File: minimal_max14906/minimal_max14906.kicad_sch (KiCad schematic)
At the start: 75 parts, among them J1 CLP-114-02-G-D-BE, J2 CLP-102-02-G-D-BE, J3 CLP-102-02-G-D-BE, J4 CLP-102-02-G-D-BE, J6 CLP-102-02-G-D-BE, J7 CLP-102-02-G-D-BE, J8 CLP-102-02-G-D-BE, Q1 SI7309DN-T1-E3, Q2 SI7309DN-T1-E3, Q3 SI7309DN-T1-E3, Q4 SI7309DN-T1-E3, U1 MAX14906ATM+

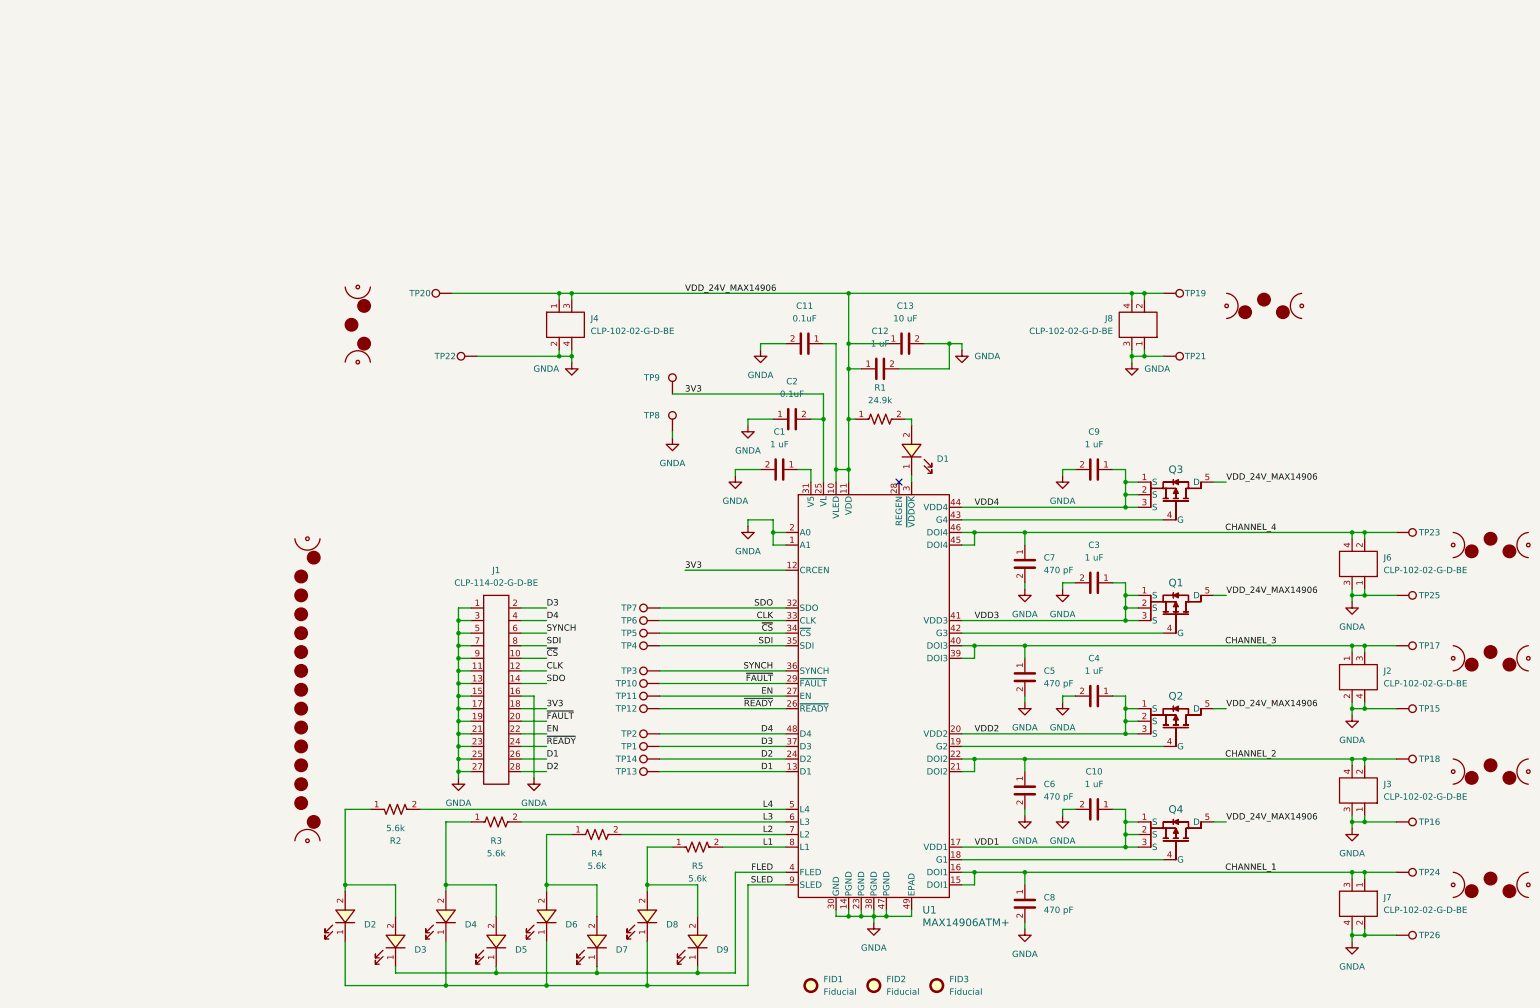
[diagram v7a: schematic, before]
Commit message: Update KiCAD schematic references for consistency and accuracy
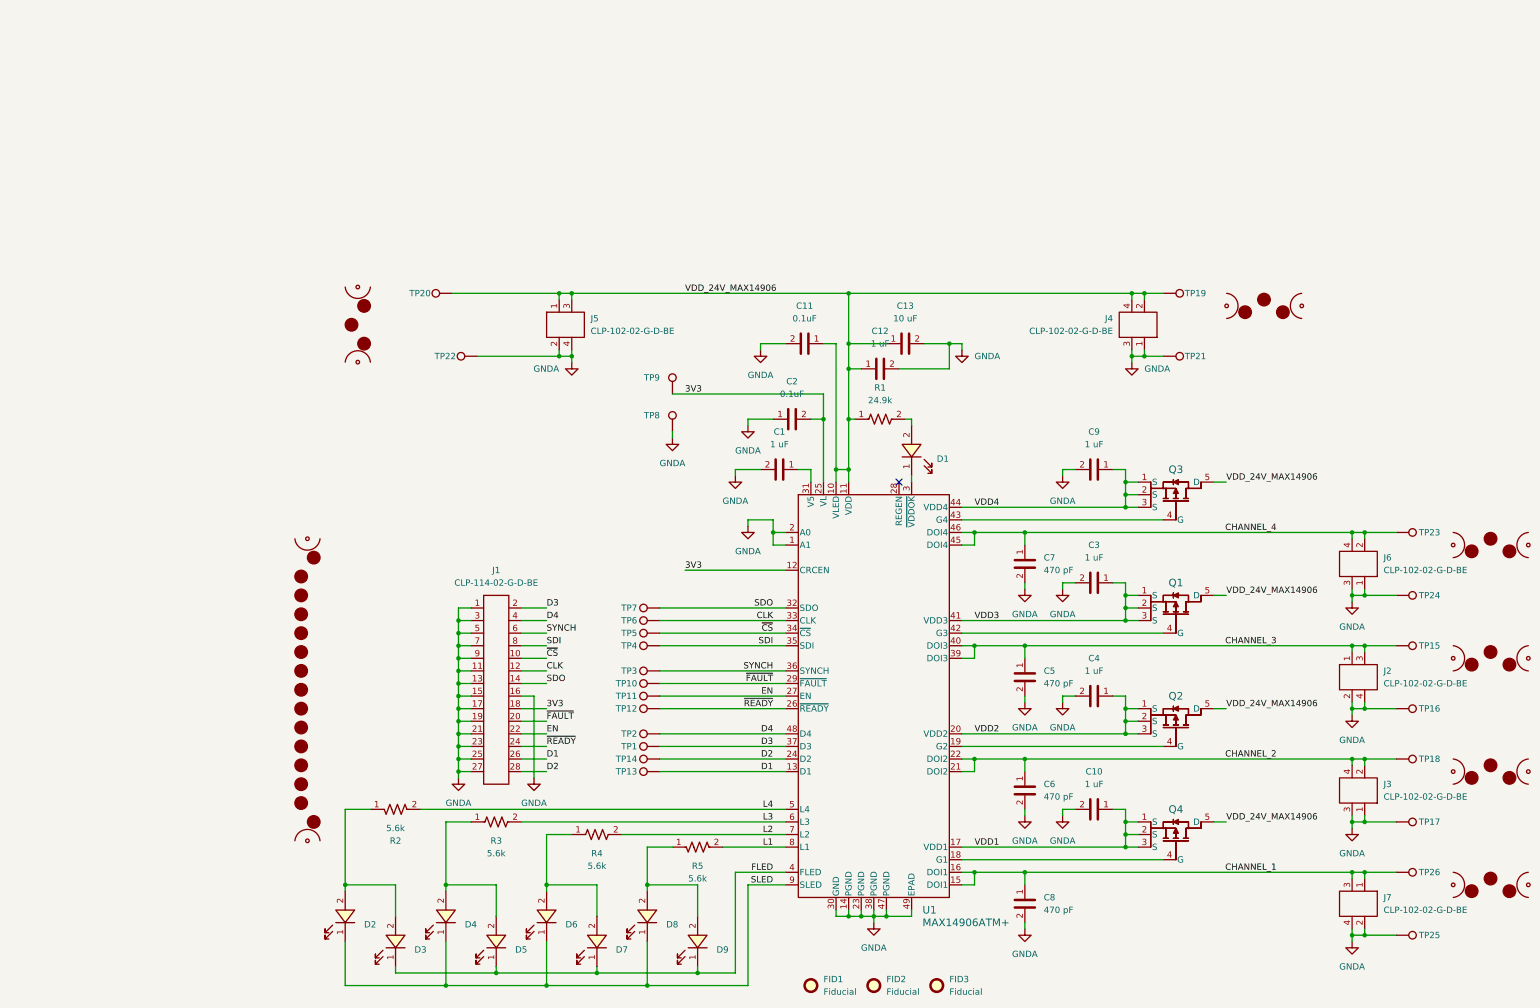
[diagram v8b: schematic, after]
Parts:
- renumbered J8 to J4, J4 to J5, MB5 to MB1, MB3 to MB2, MB1 to MB3, MB6 to MB4, MB2 to MB5, MB7 to MB6, MB4 to MB7, TP17 to TP15, TP15 to TP16, TP16 to TP17, TP25 to TP24, TP26 to TP25, TP24 to TP26
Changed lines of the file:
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@@
 		(dnp no)
 		(fields_autoplaced yes)
-		(property "Reference" "J8"
+		(property "Reference" "J4"
 			(at 264.16 76.1999 90)
 			(effects
@@
 			(project "minimal_max14906"
 				(path "/0138bc01-efaa-4f20-bf65-043bbc1a8346"
-					(reference "J8")
+					(reference "J4")
 					(unit 1)
 				)
@@
 		(dnp no)
 		(fields_autoplaced yes)
-		(property "Reference" "MB5"
+		(property "Reference" "MB1"
 			(at 106.68 151.13 0)
 			(effects
@@
 			(project ""
 				(path "/0138bc01-efaa-4f20-bf65-043bbc1a8346"
-					(reference "MB5")
+					(reference "MB1")
 					(unit 1)
 				)
@@
 		(dnp no)
 		(fields_autoplaced yes)
-		(property "Reference" "MB1"
+		(property "Reference" "MB3"
 			(at 340.36 116.84 0)
 			(effects
@@
 			(project ""
 				(path "/0138bc01-efaa-4f20-bf65-043bbc1a8346"
-					(reference "MB1")
+					(reference "MB3")
 					(unit 1)
 				)
@@
 		(on_board yes)
 		(dnp no)
-		(property "Reference" "TP26"
+		(property "Reference" "TP25"
 			(at 325.882 200.66 90)
 			(effects
@@
 			(project "minimal_max14906"
 				(path "/0138bc01-efaa-4f20-bf65-043bbc1a8346"
-					(reference "TP26")
+					(reference "TP25")
 					(unit 1)
 				)
@@
 		(dnp no)
 		(fields_autoplaced yes)
-		(property "Reference" "J4"
+		(property "Reference" "J5"
 			(at 158.75 76.1999 90)
 			(effects
@@
 			(project "minimal_max14906"
 				(path "/0138bc01-efaa-4f20-bf65-043bbc1a8346"
-					(reference "J4")
+					(reference "J5")
 					(unit 1)
 				)
@@
 		(dnp no)
 		(fields_autoplaced yes)
-		(property "Reference" "MB6"
+		(property "Reference" "MB4"
 			(at 294.64 68.58 0)
 			(effects
@@
 			(project "minimal_max14906"
 				(path "/0138bc01-efaa-4f20-bf65-043bbc1a8346"
-					(reference "MB6")
+					(reference "MB4")
 					(unit 1)
 				)
@@
 		(dnp no)
 		(fields_autoplaced yes)
-		(property "Reference" "MB4"
+		(property "Reference" "MB7"
 			(at 340.36 185.42 0)
 			(effects
@@
 			(project "minimal_max14906"
 				(path "/0138bc01-efaa-4f20-bf65-043bbc1a8346"
-					(reference "MB4")
+					(reference "MB7")
 					(unit 1)
 				)
@@
 		(on_board yes)
 		(dnp no)
-		(property "Reference" "TP16"
+		(property "Reference" "TP17"
 			(at 325.882 177.8 90)
 			(effects
@@
 			(project "minimal_max14906"
 				(path "/0138bc01-efaa-4f20-bf65-043bbc1a8346"
-					(reference "TP16")
+					(reference "TP17")
 					(unit 1)
 				)
@@
 		(on_board yes)
 		(dnp no)
-		(property "Reference" "TP24"
+		(property "Reference" "TP26"
 			(at 325.882 187.96 90)
 			(effects
@@
 			(project "minimal_max14906"
 				(path "/0138bc01-efaa-4f20-bf65-043bbc1a8346"
-					(reference "TP24")
+					(reference "TP26")
 					(unit 1)
 				)
@@
 		(dnp no)
 		(fields_autoplaced yes)
-		(property "Reference" "MB3"
+		(property "Reference" "MB2"
 			(at 340.36 162.56 0)
 			(effects
@@
 			(project "minimal_max14906"
 				(path "/0138bc01-efaa-4f20-bf65-043bbc1a8346"
-					(reference "MB3")
+					(reference "MB2")
 					(unit 1)
 				)
@@
 		(dnp no)
 		(fields_autoplaced yes)
-		(property "Reference" "MB7"
+		(property "Reference" "MB6"
 			(at 106.68 77.47 0)
 			(effects
@@
 			(project "minimal_max14906"
 				(path "/0138bc01-efaa-4f20-bf65-043bbc1a8346"
-					(reference "MB7")
+					(reference "MB6")
 					(unit 1)
 				)
@@
 		(on_board yes)
 		(dnp no)
-		(property "Reference" "TP25"
+		(property "Reference" "TP24"
 			(at 325.882 132.08 90)
 			(effects
@@
 			(project "minimal_max14906"
 				(path "/0138bc01-efaa-4f20-bf65-043bbc1a8346"
-					(reference "TP25")
+					(reference "TP24")
 					(unit 1)
 				)
@@
 		(on_board yes)
 		(dnp no)
-		(property "Reference" "TP17"
+		(property "Reference" "TP15"
 			(at 325.882 142.24 90)
 			(effects
@@
 			(project "minimal_max14906"
 				(path "/0138bc01-efaa-4f20-bf65-043bbc1a8346"
-					(reference "TP17")
+					(reference "TP15")
 					(unit 1)
 				)
@@
 		(on_board yes)
 		(dnp no)
-		(property "Reference" "TP15"
+		(property "Reference" "TP16"
 			(at 325.882 154.94 90)
 			(effects
@@
 			(project "minimal_max14906"
 				(path "/0138bc01-efaa-4f20-bf65-043bbc1a8346"
-					(reference "TP15")
+					(reference "TP16")
 					(unit 1)
 				)
@@
 		(dnp no)
 		(fields_autoplaced yes)
-		(property "Reference" "MB2"
+		(property "Reference" "MB5"
 			(at 340.36 139.7 0)
 			(effects
@@
 			(project "minimal_max14906"
 				(path "/0138bc01-efaa-4f20-bf65-043bbc1a8346"
-					(reference "MB2")
+					(reference "MB5")
 					(unit 1)
 				)
